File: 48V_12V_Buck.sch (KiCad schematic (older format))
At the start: 30 parts, among them Q4 CSD18534Q5A, Q5 CSD18540Q5B

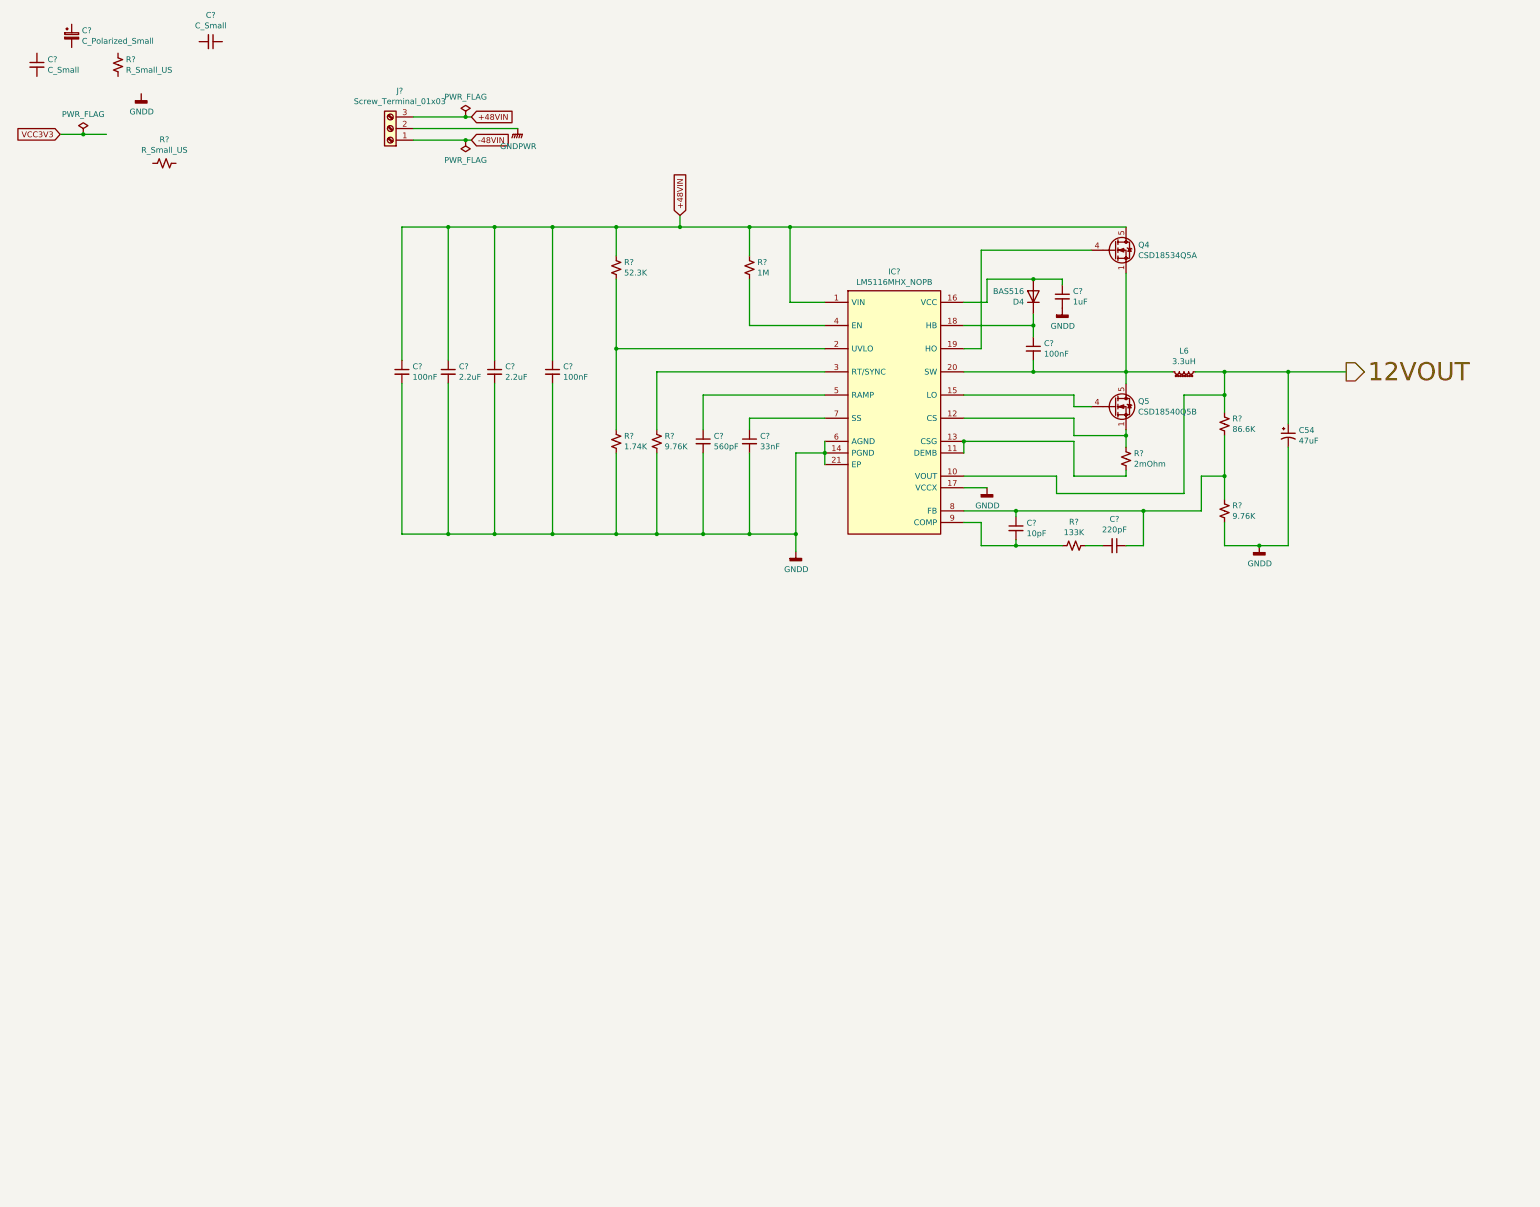
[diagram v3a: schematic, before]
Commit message: Completed USB3 1.2V Added 5V regulator cct partially completed Added BTB connector
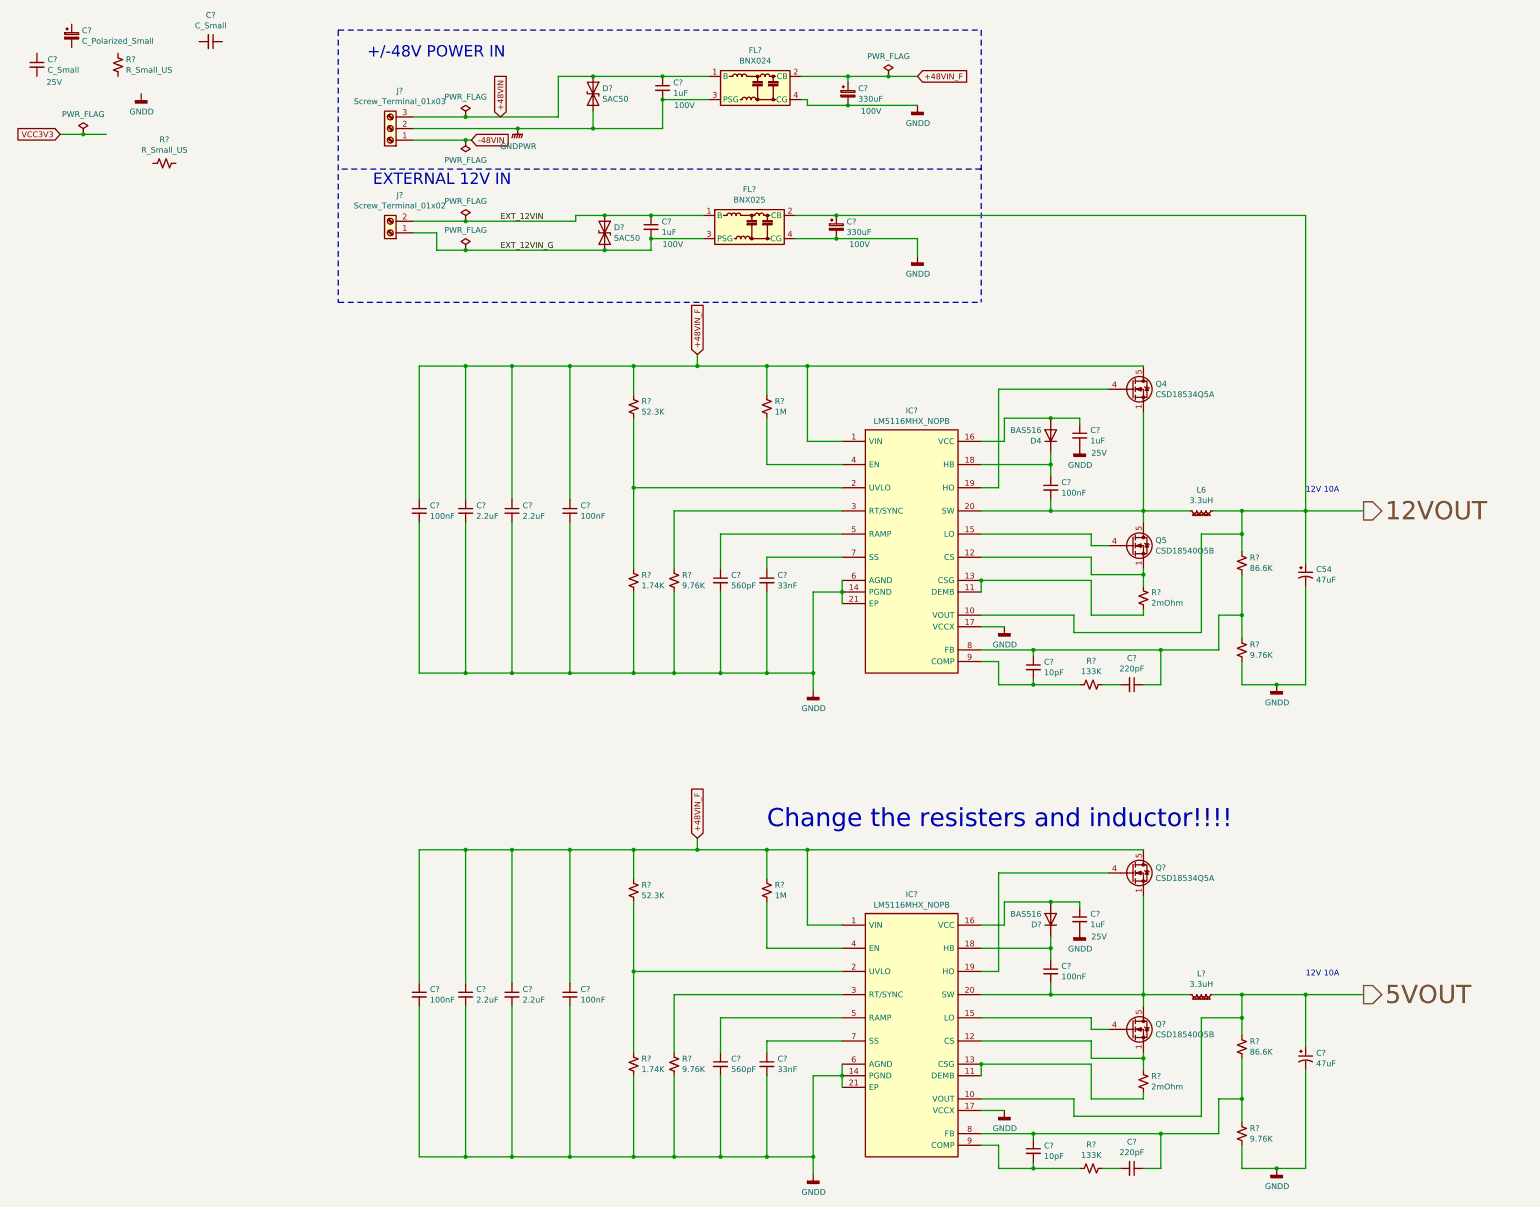
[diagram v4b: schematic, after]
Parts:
- added C? (x2): 1uF, Capacitor_SMD:C_1210_3225Metric_Pad1.33x2.70mm_HandSolder, symbol Device:C_Small
- added C? (x2): 330uF, Capacitor_SMD:CP_Elec_18x17.5, symbol Device:C_Polarized_Small
- added C?: 47uF, Capacitor_SMD:CP_Elec_6.3x5.9, symbol Device:C_Polarized_Small_US
- added C?: 33nF, Capacitor_SMD:C_0603_1608Metric_Pad1.08x0.95mm_HandSolder, symbol Device:C_Small
- added C?: 560pF, Capacitor_SMD:C_0603_1608Metric_Pad1.08x0.95mm_HandSolder, symbol Device:C_Small
- added C? (x3): 100nF, Capacitor_SMD:C_0603_1608Metric_Pad1.08x0.95mm_HandSolder, symbol Device:C_Small
- added C? (x2): 2.2uF, Capacitor_SMD:C_0603_1608Metric_Pad1.08x0.95mm_HandSolder, symbol Device:C_Small
- added C?: 1uF, Capacitor_SMD:C_0603_1608Metric_Pad1.08x0.95mm_HandSolder, symbol Device:C_Small
- added C?: 10pF, Capacitor_SMD:C_0603_1608Metric_Pad1.08x0.95mm_HandSolder, symbol Device:C_Small
- added C?: 220pF, Capacitor_SMD:C_0603_1608Metric_Pad1.08x0.95mm_HandSolder, symbol Device:C_Small
- added D? (x2): SAC50, Diode_THT:D_DO-15_P5.08mm_Vertical_AnodeUp, symbol Device:D_TVS
- added D?: BAS516, Diode_SMD:D_SOD-523, symbol Diode:BAS516
- added FL?: BNX025, Filter:Filter_Murata_BNX025, symbol Filter:BNX025
- added FL?: BNX024, GM_Filter:Filter_Murata_BNX024, symbol GM_Filters:BNX024
- added IC?: LM5116MHX_NOPB, SOP65P640X110-21N, symbol GM_Voltage_Regulators:LM5116MHX_NOPB
- added J?: Screw_Terminal_01x02, TerminalBlock:TerminalBlock_Altech_AK300-2_P5.00mm, symbol Connector:Screw_Terminal_01x02
- added L?: 3.3uH, GM_Inductors:IHLP6767GZER3R3M01, symbol Device:L_Ferrite_Small
- added Q?: CSD18534Q5A, Package_TO_SOT_SMD:TDSON-8-1, symbol Transistor_FET:CSD18534Q5A
- added Q?: CSD18540Q5B, Package_TO_SOT_SMD:TDSON-8-1, symbol Transistor_FET:CSD18540Q5B
- added R?: 1M, Resistor_SMD:R_0603_1608Metric_Pad0.98x0.95mm_HandSolder, symbol Device:R_Small_US
- added R?: 52.3K, Resistor_SMD:R_0603_1608Metric_Pad0.98x0.95mm_HandSolder, symbol Device:R_Small_US
- added R?: 1.74K, Resistor_SMD:R_0603_1608Metric_Pad0.98x0.95mm_HandSolder, symbol Device:R_Small_US
- added R? (x2): 9.76K, Resistor_SMD:R_0603_1608Metric_Pad0.98x0.95mm_HandSolder, symbol Device:R_Small_US
- added R?: 2mOhm, Resistor_SMD:R_0603_1608Metric_Pad0.98x0.95mm_HandSolder, symbol Device:R_Small_US
- added R?: 133K, Resistor_SMD:R_0603_1608Metric_Pad0.98x0.95mm_HandSolder, symbol Device:R_Small_US
- added R?: 86.6K, Resistor_SMD:R_0603_1608Metric_Pad0.98x0.95mm_HandSolder, symbol Device:R_Small_US
- C? (x2): Voltage (none) -> 25V
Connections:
- net +48VIN: now also C?.1, D?.1 (A1), FL?.1 (B); no longer C?.1, C?.1, C?.1, C?.1, IC?.1 (VIN), Q4.5 (D), R?.1, R?.1
- net 12VOUT: now also C?.1, FL?.2 (CB)
- net GNDD: now also C?.2, C?.2, C?.2, C?.2, C?.2, C?.2, C?.2, C?.2, C?.2, C?.2, FL?.4 (CG), FL?.4 (CG), IC?.14 (PGND), IC?.17 (VCCX), IC?.21 (EP), IC?.6 (AGND), R?.2, R?.2, R?.2
- net GNDPWR: now also C?.2, D?.2 (A2), FL?.3 (PSG)
- new net: C?.2, IC?.20 (SW), L?.2, Q?.1 (S), Q?.2 (S), Q?.3 (S), Q?.5 (D)
- new net: IC?.19 (HO), Q?.4 (G)
- new net: C?.1, D?.1 (K), IC?.18 (HB)
- new net: C?.1, D?.2 (A), IC?.16 (VCC)
- new net: IC?.12 (CS), Q?.1 (S), Q?.2 (S), Q?.3 (S), R?.1
- new net: IC?.15 (LO), Q?.4 (G)
- new net: IC?.11 (DEMB), IC?.13 (CSG), R?.2
- new net: IC?.2 (UVLO), R?.1, R?.2
- new net: IC?.3 (RT/SYNC), R?.1
- new net: IC?.4 (EN), R?.2
- new net: C?.1, IC?.5 (RAMP)
- new net: C?.1, IC?.7 (SS)
- new net: C?.1, C?.1, IC?.8 (FB), R?.1, R?.2
- new net: C?.2, IC?.9 (COMP), R?.2
- new net: C?.2, R?.1
- new net +48VIN_F: C?.1, C?.1, C?.1, C?.1, C?.1, C?.1, C?.1, C?.1, C?.1, FL?.2 (CB), IC?.1 (VIN), IC?.1 (VIN), Q4.5 (D), Q?.5 (D), R?.1, R?.1, R?.1, R?.1
- new net 5VOUT: C?.1, IC?.10 (VOUT), L?.1, R?.1
- new net EXT_12VIN: C?.1, D?.1 (A1), FL?.1 (B), J?.2 (Pin_2)
- new net EXT_12VIN_G: C?.2, D?.2 (A2), FL?.3 (PSG), J?.1 (Pin_1)
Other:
- note added: "+/-48V POWER IN"
- note added: "12V 10A"
- note added: "Change the resisters and inductor!!!!"
- note added: "EXTERNAL 12V IN"
- moved on the sheet: C54, C?, D4, IC?, L6, Q4, Q5, R?

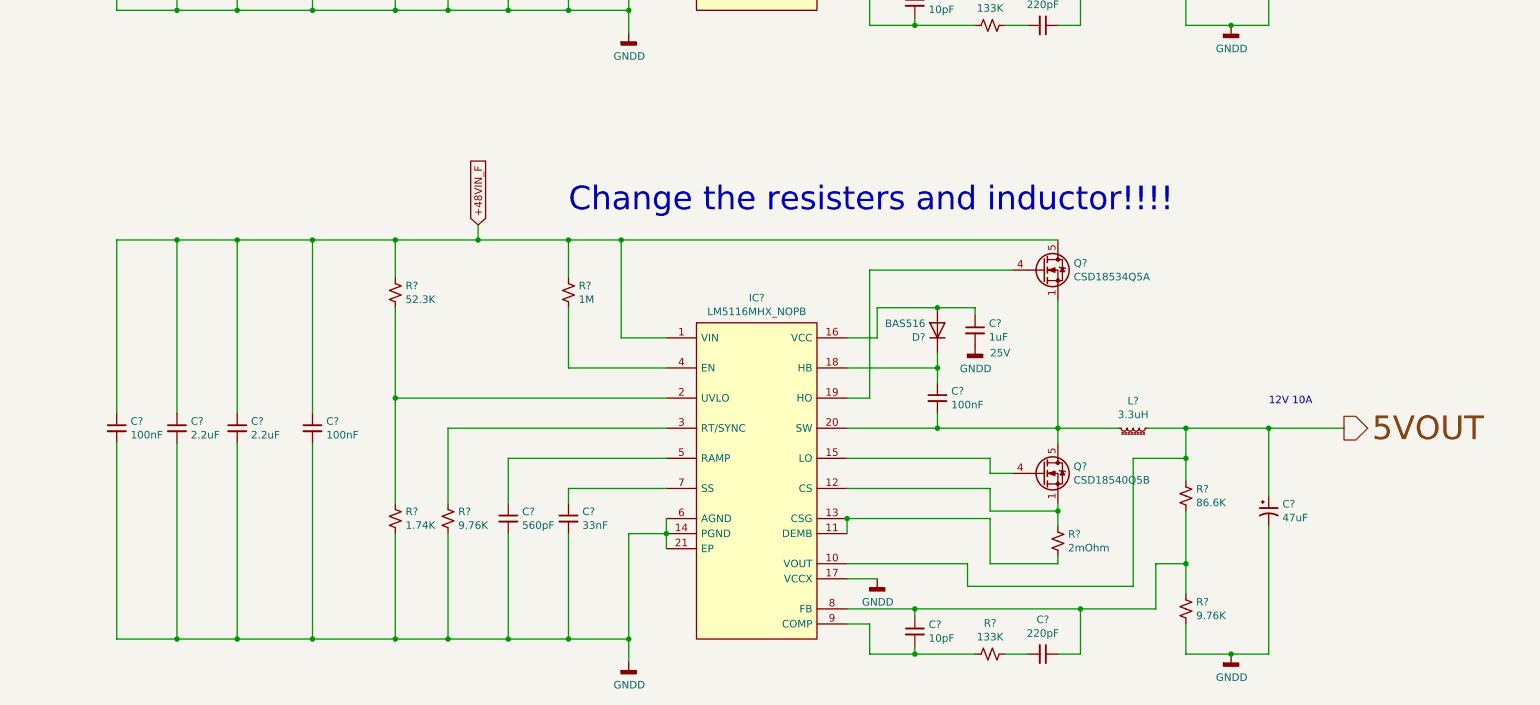
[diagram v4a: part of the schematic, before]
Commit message: Added USB3 SRAM Added 5V regulator
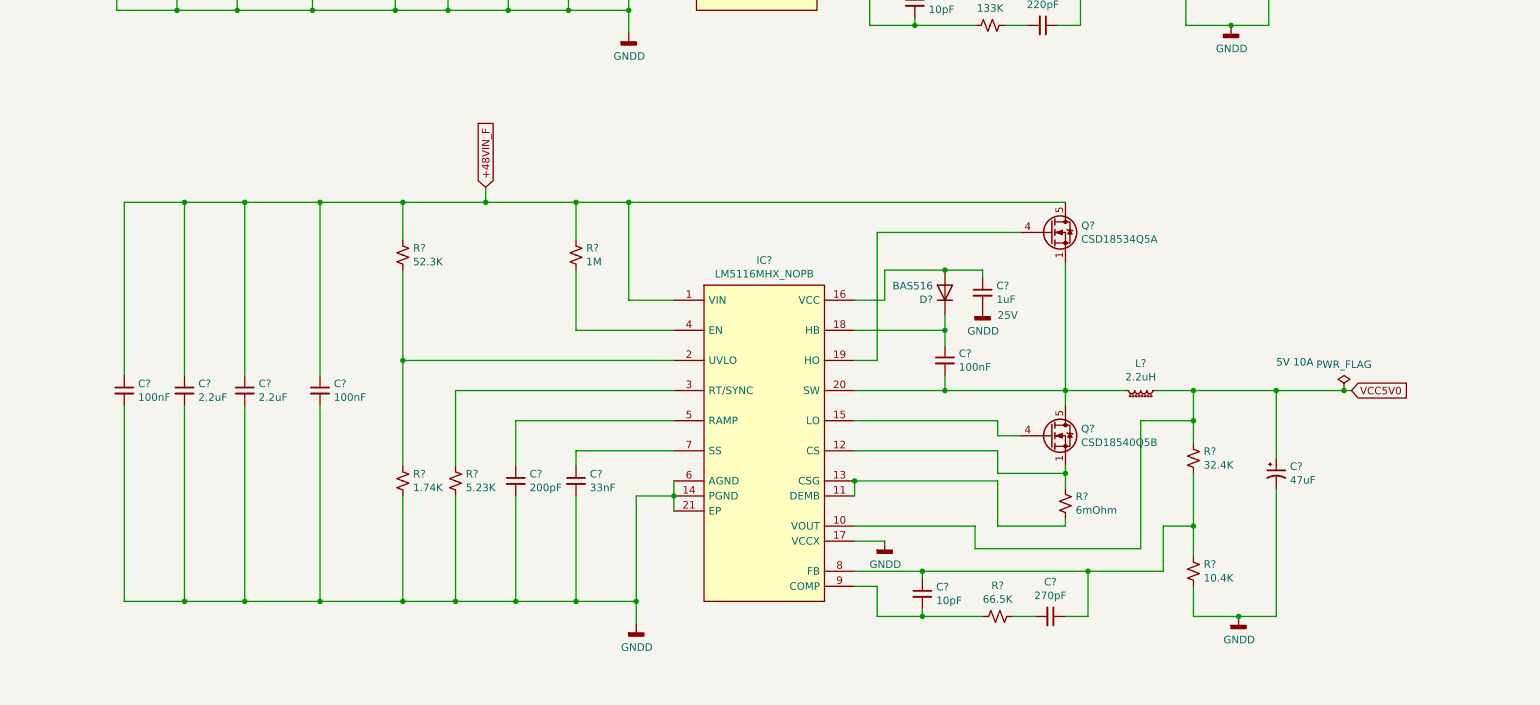
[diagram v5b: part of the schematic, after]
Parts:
- removed C?: C_Small, symbol Device:C_Small
- removed C? (x2): 560pF, Capacitor_SMD:C_0603_1608Metric_Pad1.08x0.95mm_HandSolder, symbol Device:C_Small
- removed C? (x5): 100nF, Capacitor_SMD:C_0603_1608Metric_Pad1.08x0.95mm_HandSolder, symbol Device:C_Small
- removed C? (x2): 1uF, Capacitor_SMD:C_0603_1608Metric_Pad1.08x0.95mm_HandSolder, symbol Device:C_Small
- removed C?: 330uF, Capacitor_SMD:CP_Elec_18x17.5, symbol Device:C_Polarized_Small
- removed C? (x3): 2.2uF, Capacitor_SMD:C_0603_1608Metric_Pad1.08x0.95mm_HandSolder, symbol Device:C_Small
- removed C?: 47uF, Capacitor_SMD:CP_Elec_6.3x5.9, symbol Device:C_Polarized_Small_US
- removed C?: 33nF, Capacitor_SMD:C_0603_1608Metric_Pad1.08x0.95mm_HandSolder, symbol Device:C_Small
- removed C?: 10pF, Capacitor_SMD:C_0603_1608Metric_Pad1.08x0.95mm_HandSolder, symbol Device:C_Small
- removed C?: 220pF, Capacitor_SMD:C_0603_1608Metric_Pad1.08x0.95mm_HandSolder, symbol Device:C_Small
- removed D?: SAC50, Diode_THT:D_DO-15_P5.08mm_Vertical_AnodeUp, symbol Device:D_TVS
- removed D?: BAS516, Diode_SMD:D_SOD-523, symbol Diode:BAS516
- removed FL?: BNX025, Filter:Filter_Murata_BNX025, symbol Filter:BNX025
- removed FL?: BNX024, GM_Filter:Filter_Murata_BNX024, symbol GM_Filters:BNX024
- removed IC? (x2): LM5116MHX_NOPB, SOP65P640X110-21N, symbol GM_Voltage_Regulators:LM5116MHX_NOPB
- removed J?: Screw_Terminal_01x03, TerminalBlock:TerminalBlock_Altech_AK300-3_P5.00mm, symbol Connector:Screw_Terminal_01x03
- removed L?: 3.3uH, GM_Inductors:IHLP6767GZER3R3M01, symbol Device:L_Ferrite_Small
- removed Q?: CSD18534Q5A, Package_TO_SOT_SMD:TDSON-8-1, symbol Transistor_FET:CSD18534Q5A
- removed Q?: CSD18540Q5B, Package_TO_SOT_SMD:TDSON-8-1, symbol Transistor_FET:CSD18540Q5B
- removed R? (x2): 1M, Resistor_SMD:R_0603_1608Metric_Pad0.98x0.95mm_HandSolder, symbol Device:R_Small_US
- removed R? (x2): 1.74K, Resistor_SMD:R_0603_1608Metric_Pad0.98x0.95mm_HandSolder, symbol Device:R_Small_US
- removed R? (x2): 133K, Resistor_SMD:R_0603_1608Metric_Pad0.98x0.95mm_HandSolder, symbol Device:R_Small_US
- removed R? (x2): 86.6K, Resistor_SMD:R_0603_1608Metric_Pad0.98x0.95mm_HandSolder, symbol Device:R_Small_US
- removed R?: 52.3K, Resistor_SMD:R_0603_1608Metric_Pad0.98x0.95mm_HandSolder, symbol Device:R_Small_US
- removed R? (x2): 9.76K, Resistor_SMD:R_0603_1608Metric_Pad0.98x0.95mm_HandSolder, symbol Device:R_Small_US
- removed R?: 2mOhm, Resistor_SMD:R_0603_1608Metric_Pad0.98x0.95mm_HandSolder, symbol Device:R_Small_US
- added C?: C_Small, symbol Device:C_Small
- added C?: 560pF, Capacitor_SMD:C_0603_1608Metric_Pad1.08x0.95mm_HandSolder, symbol Device:C_Small
- added C? (x5): 100nF, Capacitor_SMD:C_0603_1608Metric_Pad1.08x0.95mm_HandSolder, symbol Device:C_Small
- added C? (x2): 1uF, Capacitor_SMD:C_0603_1608Metric_Pad1.08x0.95mm_HandSolder, symbol Device:C_Small
- added C?: 330uF, Capacitor_SMD:CP_Elec_18x17.5, symbol Device:C_Polarized_Small
- added C? (x3): 2.2uF, Capacitor_SMD:C_0603_1608Metric_Pad1.08x0.95mm_HandSolder, symbol Device:C_Small
- added C?: 47uF, Capacitor_SMD:CP_Elec_6.3x5.9, symbol Device:C_Polarized_Small_US
- added C?: 33nF, Capacitor_SMD:C_0603_1608Metric_Pad1.08x0.95mm_HandSolder, symbol Device:C_Small
- added C?: 200pF, Capacitor_SMD:C_0603_1608Metric_Pad1.08x0.95mm_HandSolder, symbol Device:C_Small
- added C?: 10pF, Capacitor_SMD:C_0603_1608Metric_Pad1.08x0.95mm_HandSolder, symbol Device:C_Small
- added C?: 270pF, Capacitor_SMD:C_0603_1608Metric_Pad1.08x0.95mm_HandSolder, symbol Device:C_Small
- added D?: SAC50, Diode_THT:D_DO-15_P5.08mm_Vertical_AnodeUp, symbol Device:D_TVS
- added D?: BAS516, Diode_SMD:D_SOD-523, symbol Diode:BAS516
- added FL?: BNX025, Filter:Filter_Murata_BNX025, symbol Filter:BNX025
- added FL?: BNX024, GM_Filter:Filter_Murata_BNX024, symbol GM_Filters:BNX024
- added IC? (x2): LM5116MHX_NOPB, SOP65P640X110-21N, symbol GM_Voltage_Regulators:LM5116MHX_NOPB
- added J?: Screw_Terminal_01x03, TerminalBlock:TerminalBlock_Altech_AK300-3_P5.00mm, symbol Connector:Screw_Terminal_01x03
- added L?: 2.2uH, GM_Inductors:L_Coilcraft_XxL7070, symbol Device:L_Ferrite_Small
- added Q?: CSD18534Q5A, Package_TO_SOT_SMD:TDSON-8-1, symbol Transistor_FET:CSD18534Q5A
- added Q?: CSD18540Q5B, Package_TO_SOT_SMD:TDSON-8-1, symbol Transistor_FET:CSD18540Q5B
- added R? (x2): 1M, Resistor_SMD:R_0603_1608Metric_Pad0.98x0.95mm_HandSolder, symbol Device:R_Small_US
- added R? (x2): 1.74K, Resistor_SMD:R_0603_1608Metric_Pad0.98x0.95mm_HandSolder, symbol Device:R_Small_US
- added R?: 133K, Resistor_SMD:R_0603_1608Metric_Pad0.98x0.95mm_HandSolder, symbol Device:R_Small_US
- added R?: 86.6K, Resistor_SMD:R_0603_1608Metric_Pad0.98x0.95mm_HandSolder, symbol Device:R_Small_US
- added R?: 52.3K, Resistor_SMD:R_0603_1608Metric_Pad0.98x0.95mm_HandSolder, symbol Device:R_Small_US
- added R?: 5.23K, Resistor_SMD:R_0603_1608Metric_Pad0.98x0.95mm_HandSolder, symbol Device:R_Small_US
- added R?: 6mOhm, Resistor_SMD:R_0603_1608Metric_Pad0.98x0.95mm_HandSolder, symbol Device:R_Small_US
- added R?: 66.5K, Resistor_SMD:R_0603_1608Metric_Pad0.98x0.95mm_HandSolder, symbol Device:R_Small_US
- added R?: 32.4K, Resistor_SMD:R_0603_1608Metric_Pad0.98x0.95mm_HandSolder, symbol Device:R_Small_US
- added R?: 10.4K, Resistor_SMD:R_0603_1608Metric_Pad0.98x0.95mm_HandSolder, symbol Device:R_Small_US
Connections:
- net +48VIN: now also D?.1 (A1), FL?.1 (B), J?.3 (Pin_3)
- net +48VIN_F: now also C?.1, C?.1, C?.1, C?.1, C?.1, C?.1, C?.1, FL?.2 (CB), IC?.1 (VIN), IC?.1 (VIN), Q?.5 (D), R?.1, R?.1, R?.1
- net -48VIN: now also J?.1 (Pin_1)
- net 12VOUT: now also FL?.2 (CB), IC?.10 (VOUT), R?.1
- net EXT_12VIN: now also FL?.1 (B)
- net EXT_12VIN_G: now also FL?.3 (PSG)
- net GNDD: now also C?.2, C?.2, C?.2, C?.2, C?.2, C?.2, C?.2, C?.2, C?.2, C?.2, C?.2, C?.2, C?.2, FL?.4 (CG), FL?.4 (CG), IC?.14 (PGND), IC?.14 (PGND), IC?.17 (VCCX), IC?.17 (VCCX), IC?.21 (EP), IC?.21 (EP), IC?.6 (AGND), IC?.6 (AGND), R?.2, R?.2, R?.2, R?.2
- net GNDPWR: now also D?.2 (A2), FL?.3 (PSG), J?.2 (Pin_2)
- net at L6.2, Q4.1 (S), Q4.2 (S)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: now also C?.2, IC?.20 (SW)
- net at Q4.4 (G): now also IC?.19 (HO)
- net at D4.1 (K): now also C?.1, IC?.18 (HB)
- net at D4.2 (A): now also C?.1, IC?.16 (VCC)
- net at Q5.1 (S), Q5.2 (S), Q5.3 (S)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: now also IC?.12 (CS)
- net at Q5.4 (G): now also IC?.15 (LO)
- net at R?.2: now also IC?.11 (DEMB), IC?.13 (CSG)
- net at R?.2: now also IC?.2 (UVLO), R?.1
- net at R?.1: now also IC?.3 (RT/SYNC)
- net at C?.1: now also IC?.7 (SS)
- net at C?.1, C?.1, R?.1: now also IC?.8 (FB), R?.2
- net at C?.2: now also IC?.9 (COMP), R?.2
- net at C?.2: now also R?.1
- new net: IC?.4 (EN), R?.2 (x2)
- new net: C?.1, IC?.5 (RAMP) (x2)
- new net: C?.2, IC?.20 (SW), L?.2, Q?.1 (S), Q?.2 (S), Q?.3 (S), Q?.5 (D)
- new net: IC?.19 (HO), Q?.4 (G)
- new net: C?.1, D?.1 (K), IC?.18 (HB)
- new net: C?.1, D?.2 (A), IC?.16 (VCC)
- new net: IC?.12 (CS), Q?.1 (S), Q?.2 (S), Q?.3 (S), R?.1
- new net: IC?.15 (LO), Q?.4 (G)
- new net: IC?.11 (DEMB), IC?.13 (CSG), R?.2
- new net: IC?.2 (UVLO), R?.1, R?.2
- new net: IC?.3 (RT/SYNC), R?.1
- new net: C?.1, IC?.7 (SS)
- new net: C?.1, C?.1, IC?.8 (FB), R?.1, R?.2
- new net: C?.2, IC?.9 (COMP), R?.2
- new net: C?.2, R?.1
- new net VCC5V0: C?.1, IC?.10 (VOUT), L?.1, R?.1
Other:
- note added: "5V 10A"
- note removed: "Change the resisters and inductor!!!!"
